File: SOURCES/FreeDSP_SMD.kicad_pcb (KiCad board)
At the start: 2 copper layers, 100 x 100 mm, 163 parts, among them IC1 AD8608, IC2 ADAU1701, IC3 24AA256, IC4 TC7SZ08, IC5 AD8608, IC6 AD8608, P1 CONN_02X11, P10 CONN_02X10, P2 CONN_2, P3 CONN_02X02, P4 USBi, P5 CONN_02X13, P6 CONN_01X06, P7 CONN_01X06, P8 CONN_01X06, P9 CONN_02X10, Q1 PNP, Q2 2N7000, Q3 2N7000, U1 78033, U2 4040, U3 7805, X1 12M288Hz

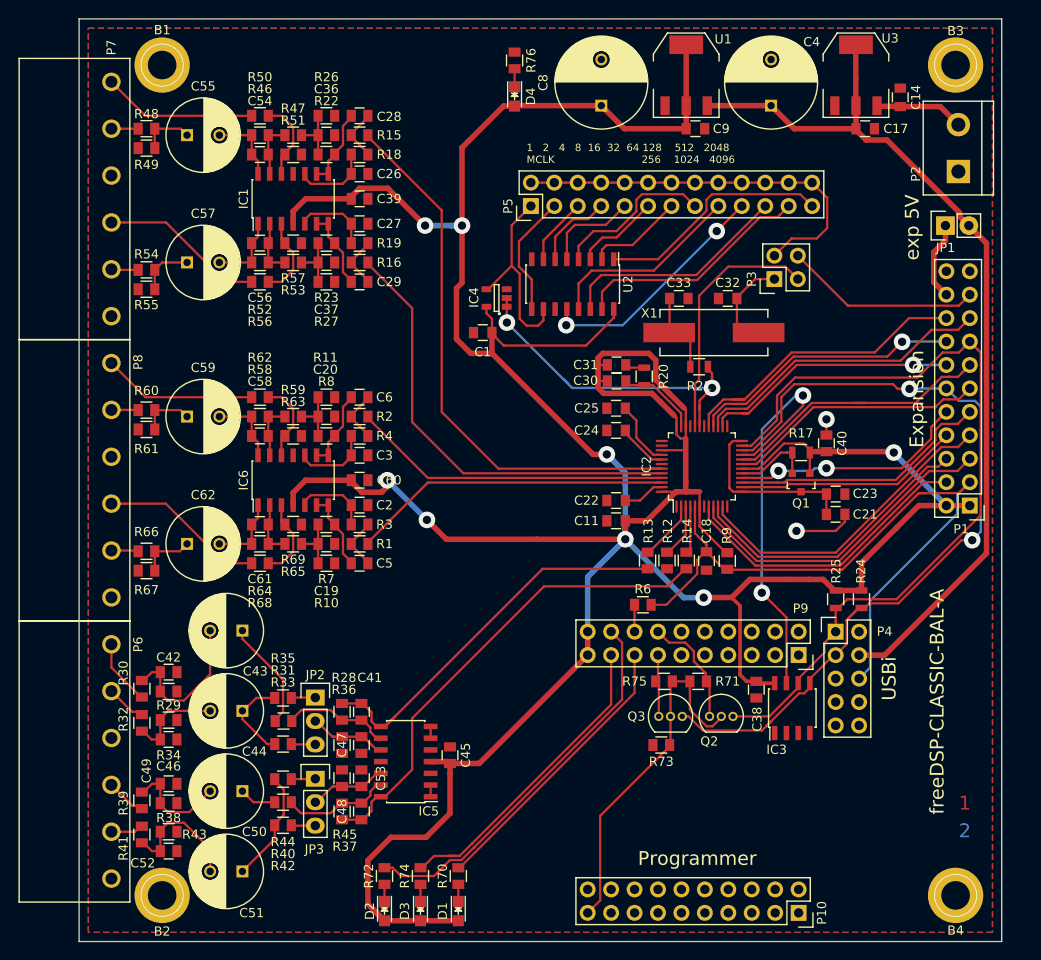
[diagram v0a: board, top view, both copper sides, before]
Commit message: Cleaned BOM (footprints).
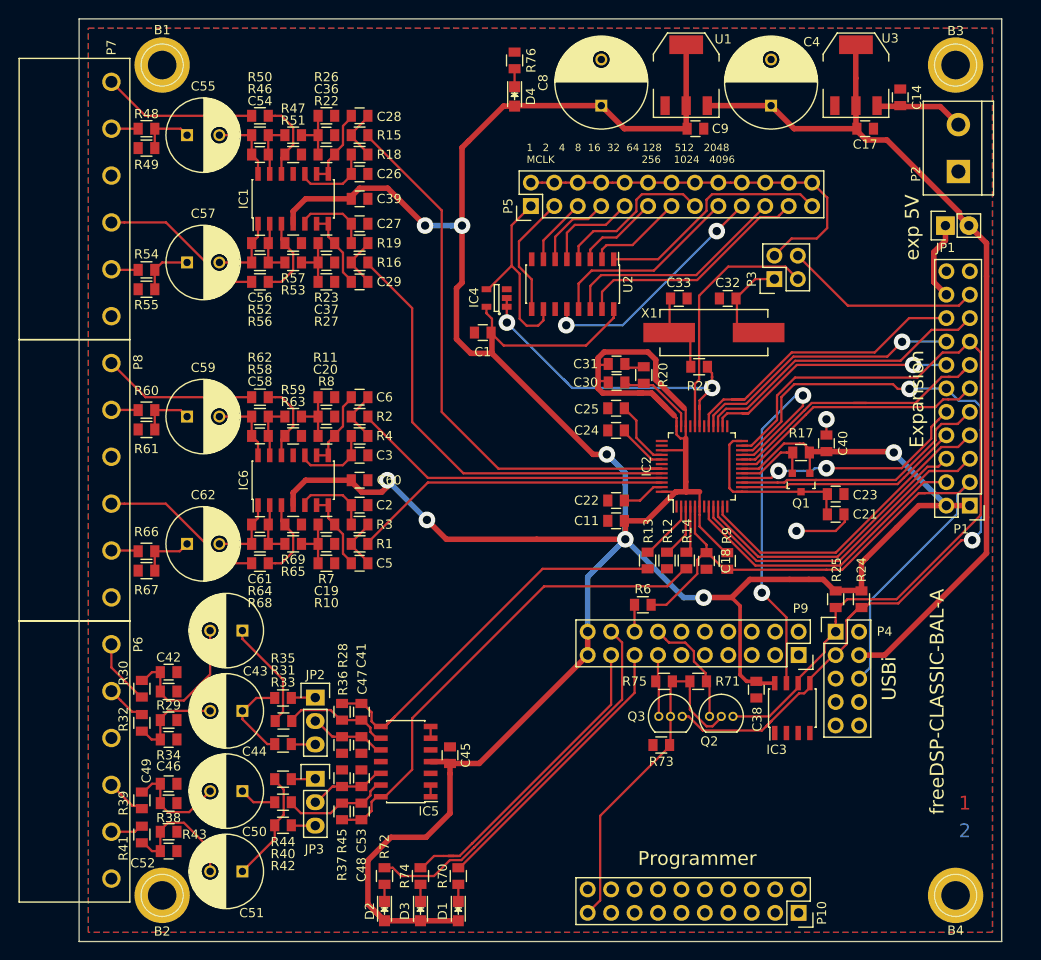
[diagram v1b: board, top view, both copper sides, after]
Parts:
- C1, C17, C23: footprint Capacitors_SMD:C_0805 -> rklib:C0805-X7R
- C11, C14, C21, C22, C24, C25, C9: value 10u -> 10u0; footprint Capacitors_SMD:C_0805 -> rklib:C0805-X7R
- C18: value 10n -> 10n0; footprint Capacitors_SMD:C_0805 -> rklib:C0805-X7R
- C19, C20, C36, C37: value 3n3 -> 3n30
- C30: value 3n3 -> 3n30; footprint Capacitors_SMD:C_0805 -> rklib:C0805-X7R
- C31: value 56n -> 56n0; footprint Capacitors_SMD:C_0805 -> rklib:C0805-X7R
- C32, C33: value 22p -> 22p0; footprint Capacitors_SMD:C_0805 -> rklib:C0805-X7R
- Q1: value PNP -> ZXTP25040DFHTA
- R1, R15, R16, R18, R19, R2, R3, R4: value 4k75 -> 4K75
- R10, R11, R26, R27: value 47k -> 47K0
- R12, R13, R14, R9: value 18k -> 18K0
- R17: value 1k -> 1K00; footprint Resistors_SMD:R_0805 -> rklib:C0805-RES
- R20, R21: footprint Resistors_SMD:R_0805 -> rklib:C0805-RES
- R22, R23, R7, R8: value 680 -> 680R
- R24, R25: value 10k -> 10K0; footprint Resistors_SMD:R_0805 -> rklib:C0805-RES
- R28, R36, R37, R45, R46, R47, R52, R53, R58, R59, R64, R65, R71, R75: value 10k -> 10K0
- R29, R34, R38, R43: value 100k -> 100K
- R31, R33, R40, R42: value 20k -> 20K0
- R49, R55, R61, R67: value 22k -> 22K0
- moved R20 0.16 mm to (161.2, 88.6)
- moved C30 0.15 mm to (158.2, 89.4)
- moved C31 0.10 mm to (158.2, 87.4)
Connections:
- P10 pad 1: (no net) -> /PD3
- P10 pad 10: (no net) -> /PA4
- P10 pad 11: (no net) -> /USB_COUT
- P10 pad 12: (no net) -> /~USB_CLATCH1
- P10 pad 13: (no net) -> /CTL2
- P10 pad 14: (no net) -> /USB_CDATA
- P10 pad 15: (no net) -> /CTL0
- P10 pad 16: (no net) -> /CTL1
- P10 pad 17: (no net) -> /PB6
- P10 pad 18: (no net) -> /PB7
- P10 pad 2: (no net) -> /PD4
- P10 pad 20: (no net) -> /PB5
- P10 pad 3: (no net) -> /PD1
- P10 pad 4: (no net) -> /PD2
- P10 pad 5: (no net) -> /USB_CCLK
- P10 pad 6: (no net) -> /PD0
- P10 pad 7: (no net) -> /PA5
- P10 pad 8: (no net) -> /PA6
- P10 pad 9: (no net) -> /PA3
- P4 pad 2: (no net) -> Net-(P4-Pad2)
- P4 pad 5: (no net) -> Net-(P4-Pad5)
- P4 pad 7: (no net) -> Net-(P4-Pad7)
- P4 pad 8: (no net) -> Net-(P4-Pad8)
- P4 pad 9: (no net) -> Net-(P4-Pad9)
- P9 pad 1: (no net) -> /PD6
- P9 pad 11: (no net) -> /IFCLK
- P9 pad 2: (no net) -> /PD5
- P9 pad 4: (no net) -> /PD7
- P9 pad 6: (no net) -> /USB_CLK
- P9 pad 7: (no net) -> /RDY1
- P9 pad 8: (no net) -> /RDY0
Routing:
- net 3V3: track 399.6 -> 402.2 mm

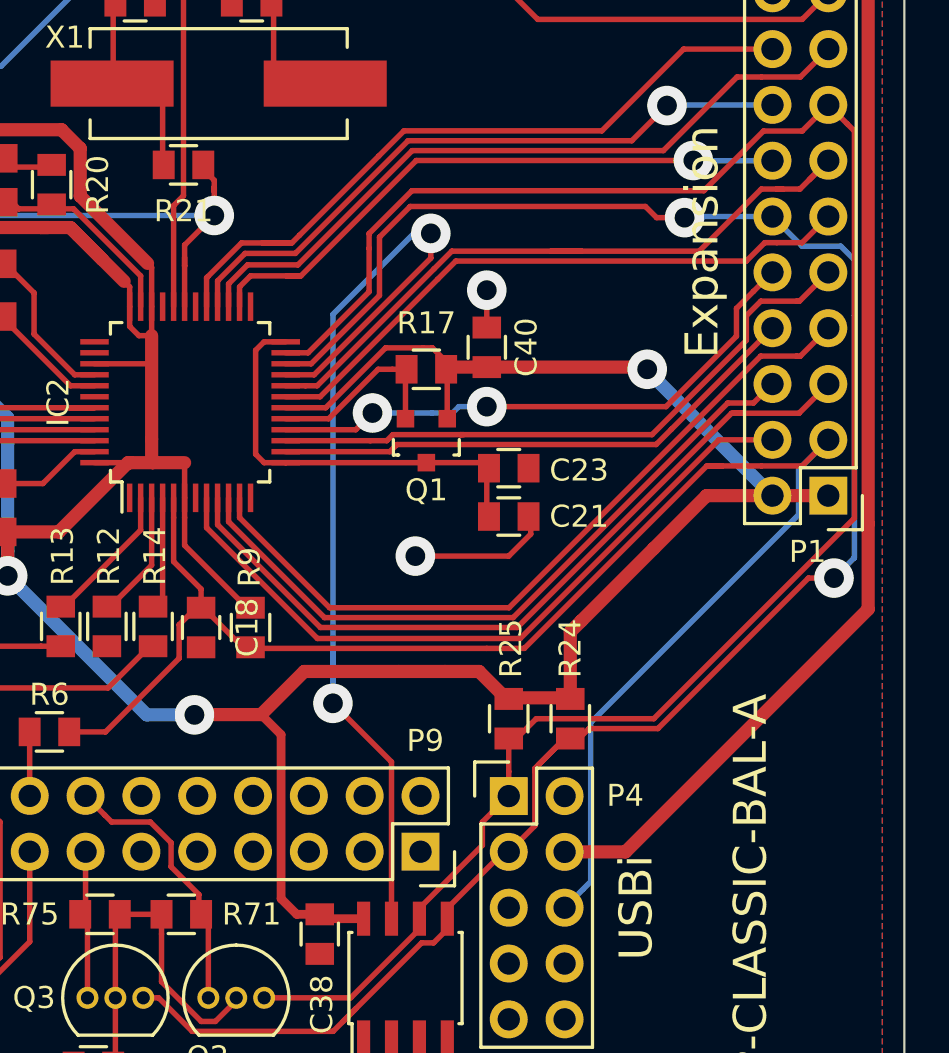
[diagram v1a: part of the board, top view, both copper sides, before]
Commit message: - Added 10K PullUp and GND-Jumper on WP-line - Fixed footprint of Q1
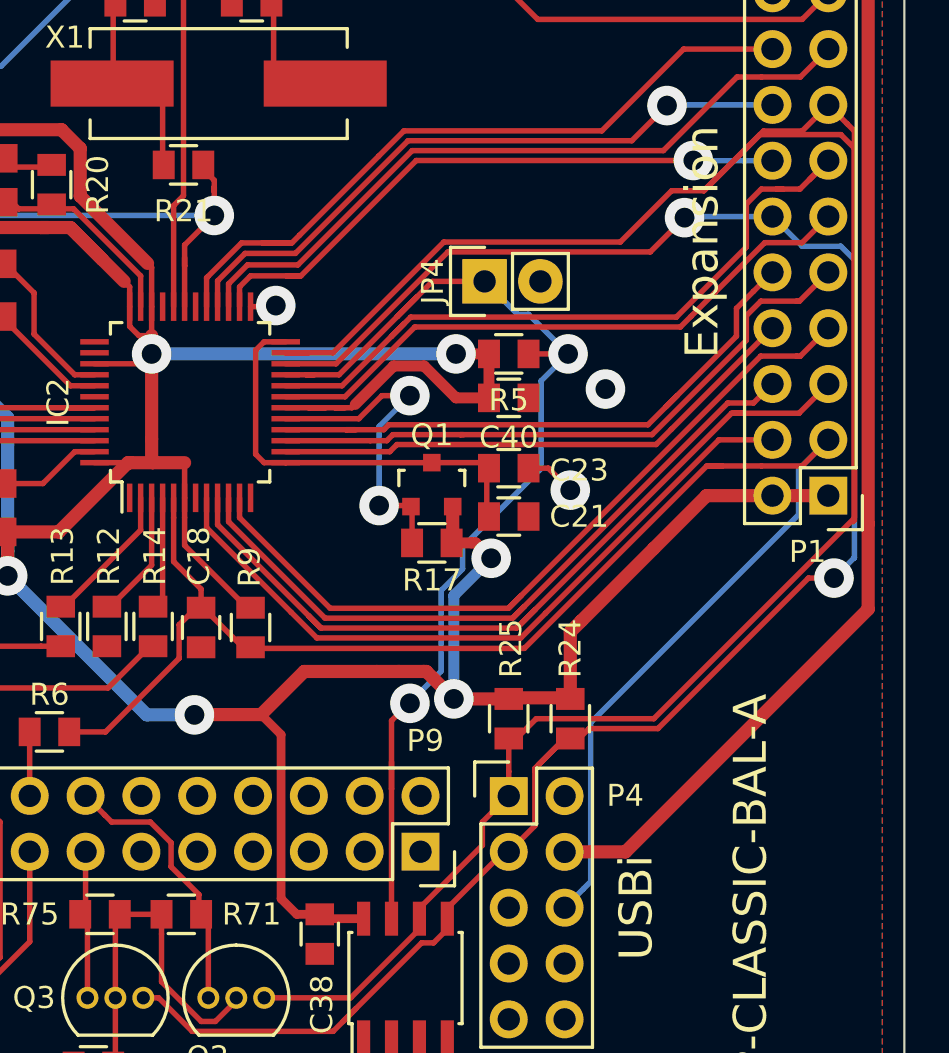
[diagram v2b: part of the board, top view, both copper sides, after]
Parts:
- added JP4: JUMPER, Pin_Headers:Pin_Header_Straight_1x02, F.Cu at (180.9, 93.0)
- added R5: 10K0, rklib:C0805-RES, F.Cu at (182.0, 96.3)
- moved R17 7.90 mm to (178.5, 104.9)
- moved C40 2.51 mm to (182.0, 98.3), turned to 0 degrees
- moved Q1 2.01 mm to (178.5, 102.2), turned to 0 degrees
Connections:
- Q1 pad 1: 3V3 -> Net-(IC2-Pad17)
- Q1 pad 2: Net-(IC2-Pad17) -> 3V3
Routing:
- net SCL: track 88.8 -> 113.5 mm
- net 3V3: track 402.2 -> 416.0 mm, vias 8 -> 11
- net Net-(IC2-Pad17): track 8.63 -> 14.8 mm, vias 0 -> 2
- net GND: track 8.36 -> 3.48 mm
- net /WP: track 46.2 -> 49.7 mm
- net SDA: track 91.6 -> 89.7 mm
- net MP5: track 35.9 -> 37.8 mm
- net MP10: track 25.9 -> 27.0 mm, vias 2 -> 0
- net MP0: track 34.7 -> 35.5 mm
- net MP1: track 32.0 -> 32.8 mm
- net WB: track 31.8 -> 32.4 mm
- net (no net): vias 0 -> 1

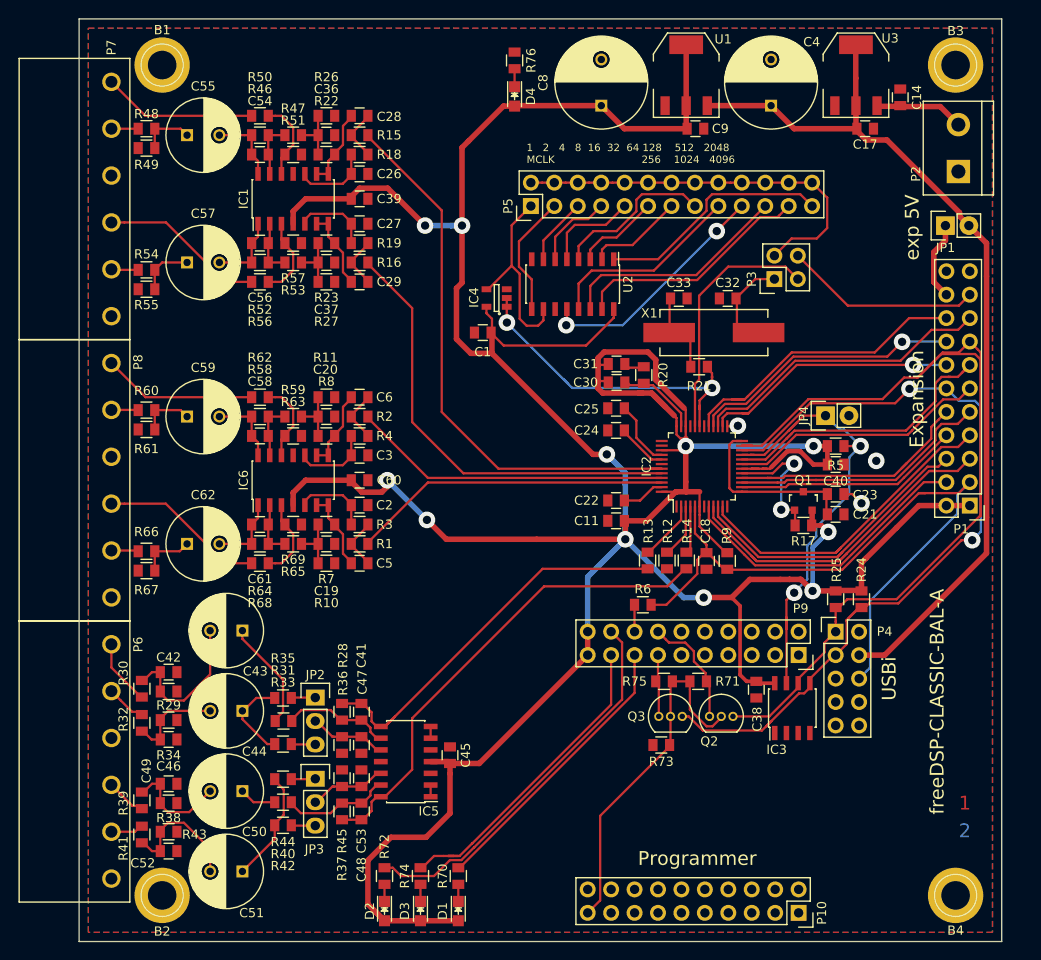
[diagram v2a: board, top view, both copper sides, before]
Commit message: - Bugfix ADC-Stage: Applied VCC/2 - Changed VCC of OpAmps to +5V - Changed gains, Pro: +6dBu (ARD-Norm) and Con: -10dBv for full scale
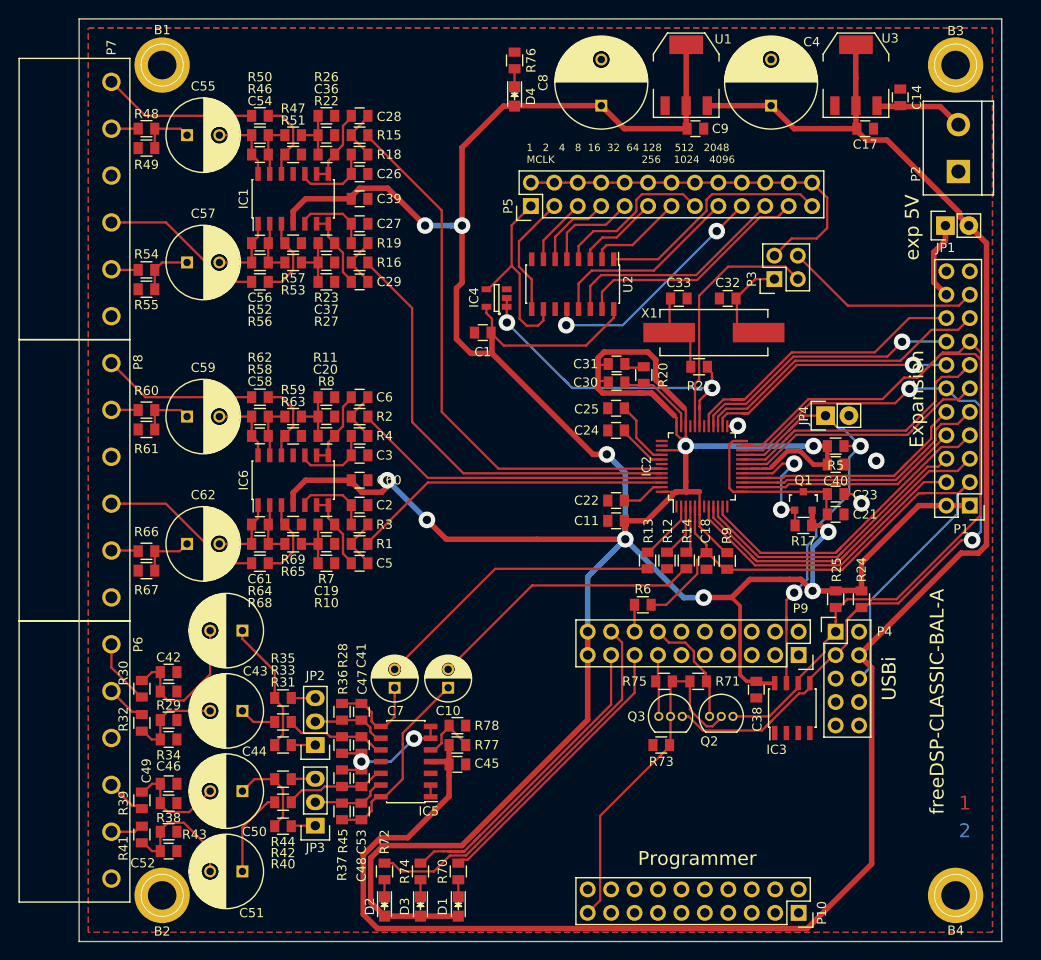
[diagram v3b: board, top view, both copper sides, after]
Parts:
- added C10: 47u0./16V, Capacitors_ThroughHole:C_Radial_D5_L11_P2, F.Cu at (140.0, 122.5)
- added C7: 47u0./16V, Capacitors_ThroughHole:C_Radial_D5_L11_P2, F.Cu at (134.2, 122.5)
- added R77: 47K0, rklib:C0805-RES, F.Cu at (141.0, 128.7)
- added R78: 47K0, rklib:C0805-RES, F.Cu at (141.0, 126.6)
- C43, C44, C50, C51: value 47u0 ./ 35V -> 47u0./35V
- IC5: value AD8608 -> AD8608ARZ
- R13, R14: value 18K0 -> 7K15
- R31, R33, R40, R42: value 20K0 -> 17K4
- R35, R44: value 100R -> 3K57
- moved JP2 5.14 mm to (125.6, 128.7), turned to 180 degrees
- moved JP3 5.08 mm to (125.6, 137.4), turned to 180 degrees
- moved R31 2.60 mm to (122.1, 128.7)
- moved R40 2.60 mm to (122.1, 137.5)
- moved R42 2.50 mm to (122.1, 134.9)
- moved R33 2.40 mm to (122.1, 126.2)
- moved C45 1.28 mm to (141.0, 130.8), turned to 180 degrees
- moved D1 0.50 mm to (141.1, 146.2)
- moved D2 0.50 mm to (133.1, 146.2)
- moved D3 0.50 mm to (137.0, 146.2)
- moved R70 0.50 mm to (141.1, 142.4)
- moved R72 0.50 mm to (133.1, 142.4)
- moved R74 0.50 mm to (137.0, 142.4)
- turned C47 to 270 degrees
- turned C53 to 90 degrees
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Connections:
- C41 pad 1: /IN1 -> Net-(C41-Pad1)
- C45 pad 2: 3V3 -> +5V
- C47 pad 1: GND -> Net-(C47-Pad1)
- C47 pad 2: Net-(C47-Pad2) -> /Vcom
- C48 pad 1: /IN2 -> Net-(C10-Pad1)
- C53 pad 1: GND -> Net-(C53-Pad1)
- C53 pad 2: Net-(C53-Pad2) -> /Vcom
- IC5 pad 10: Net-(C47-Pad2) -> Net-(C47-Pad1)
- IC5 pad 12: Net-(C53-Pad2) -> Net-(C53-Pad1)
- IC5 pad 14: /IN2 -> Net-(C10-Pad1)
- IC5 pad 4: 3V3 -> +5V
- IC5 pad 5: GND -> Net-(IC5-Pad5)
- IC5 pad 6: Net-(IC5-Pad6) -> /Vcom
- IC5 pad 7: Net-(IC5-Pad6) -> /Vcom
- IC5 pad 8: /IN1 -> Net-(C41-Pad1)
- JP2 pad 2: Net-(C47-Pad2) -> Net-(C41-Pad2)
- JP3 pad 2: Net-(C53-Pad2) -> Net-(C48-Pad2)
- P6 pad 1: /IN1- -> /IN1+
- P6 pad 2: /IN1+ -> /IN1-
- P6 pad 4: /IN2- -> /IN2+
- P6 pad 5: /IN2+ -> /IN2-
- R28 pad 1: /IN1 -> Net-(C41-Pad1)
- R30 pad 2: /IN1- -> /IN1+
- R31 pad 1: Net-(C41-Pad2) -> Net-(JP2-Pad1)
- R32 pad 2: /IN1+ -> /IN1-
- R33 pad 1: Net-(JP2-Pad3) -> Net-(C47-Pad1)
- R35 pad 1: Net-(JP2-Pad1) -> Net-(JP2-Pad3)
- R35 pad 2: Net-(C44-Pad1) -> Net-(C43-Pad1)
- R36 pad 1: GND -> Net-(C47-Pad1)
- R36 pad 2: Net-(C47-Pad2) -> /Vcom
- R37 pad 1: /IN2 -> Net-(C10-Pad1)
- R39 pad 2: /IN2- -> /IN2+
- R40 pad 1: Net-(C48-Pad2) -> Net-(JP3-Pad1)
- R41 pad 2: /IN2+ -> /IN2-
- R42 pad 1: Net-(JP3-Pad3) -> Net-(C53-Pad1)
- R44 pad 1: Net-(JP3-Pad1) -> Net-(JP3-Pad3)
- R44 pad 2: Net-(C51-Pad1) -> Net-(C50-Pad1)
- R45 pad 1: GND -> Net-(C53-Pad1)
- R45 pad 2: Net-(C53-Pad2) -> /Vcom
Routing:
- net +5V: track 100.3 -> 207.7 mm
- net /IN2: track 52.4 -> 30.3 mm
- net Net-(C10-Pad1): track 0.00 -> 20.9 mm
- net SCL: track 113.5 -> 96.4 mm
- net /Vcom: track 0.00 -> 15.8 mm, vias 0 -> 2
- net Net-(C47-Pad1): track 0.00 -> 11.6 mm
- net /IN1: track 43.3 -> 31.9 mm
- net Net-(C53-Pad1): track 0.00 -> 11.1 mm
- net Net-(C41-Pad1): track 0.00 -> 10.9 mm
- net Net-(C53-Pad2): track 8.55 -> 0.00 mm
- net Net-(C47-Pad2): track 8.40 -> 0.00 mm
- net Net-(IC5-Pad5): track 0.00 -> 6.42 mm
- net Net-(C50-Pad1): track 4.00 -> 9.88 mm
- net Net-(C44-Pad1): track 9.60 -> 4.10 mm
- net 3V3: track 416.0 -> 412.3 mm
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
